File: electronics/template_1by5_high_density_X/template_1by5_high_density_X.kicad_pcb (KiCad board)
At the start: 2 copper layers, 19 x 41.5 mm, 14 parts, among them J1 1, J10 10, J11 11, J12 12, J2 2, J3 3, J4 4, J5 5, J6 6, J7 7, J8 8, J9 9

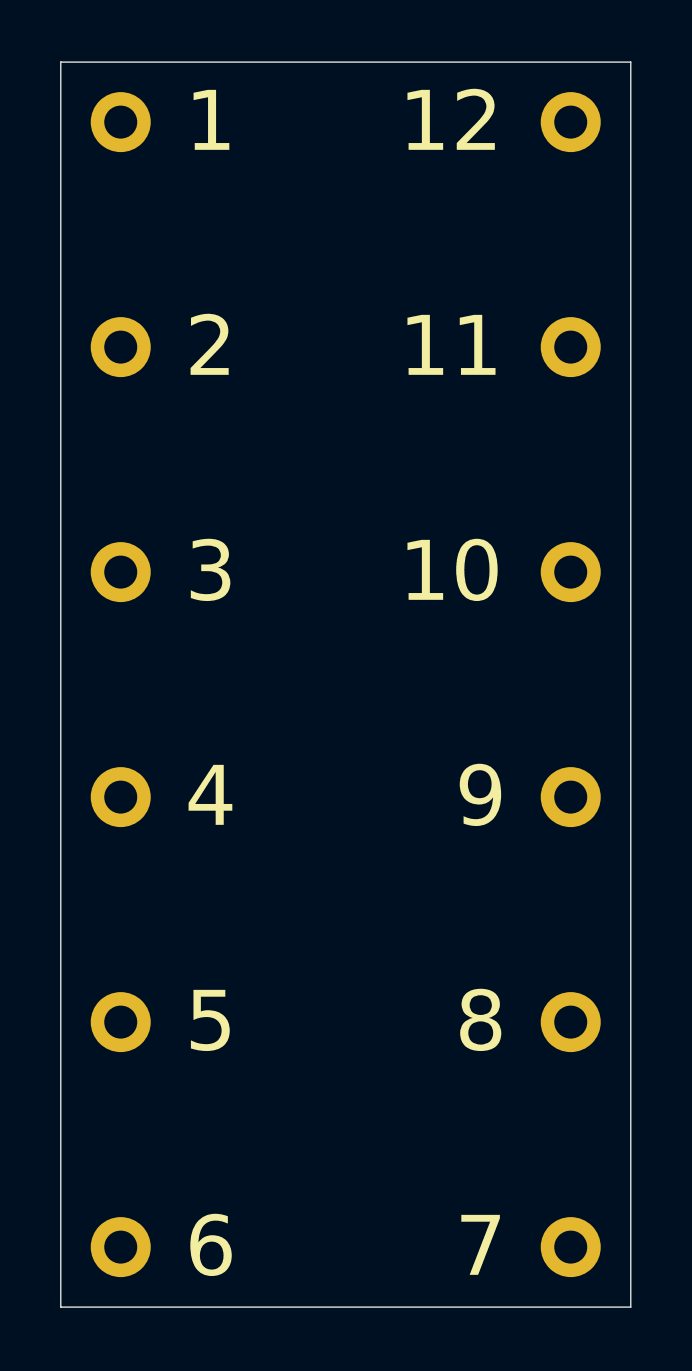
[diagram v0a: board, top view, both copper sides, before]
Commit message: completed high density X templates, updated versionnumbers of high density XN templates
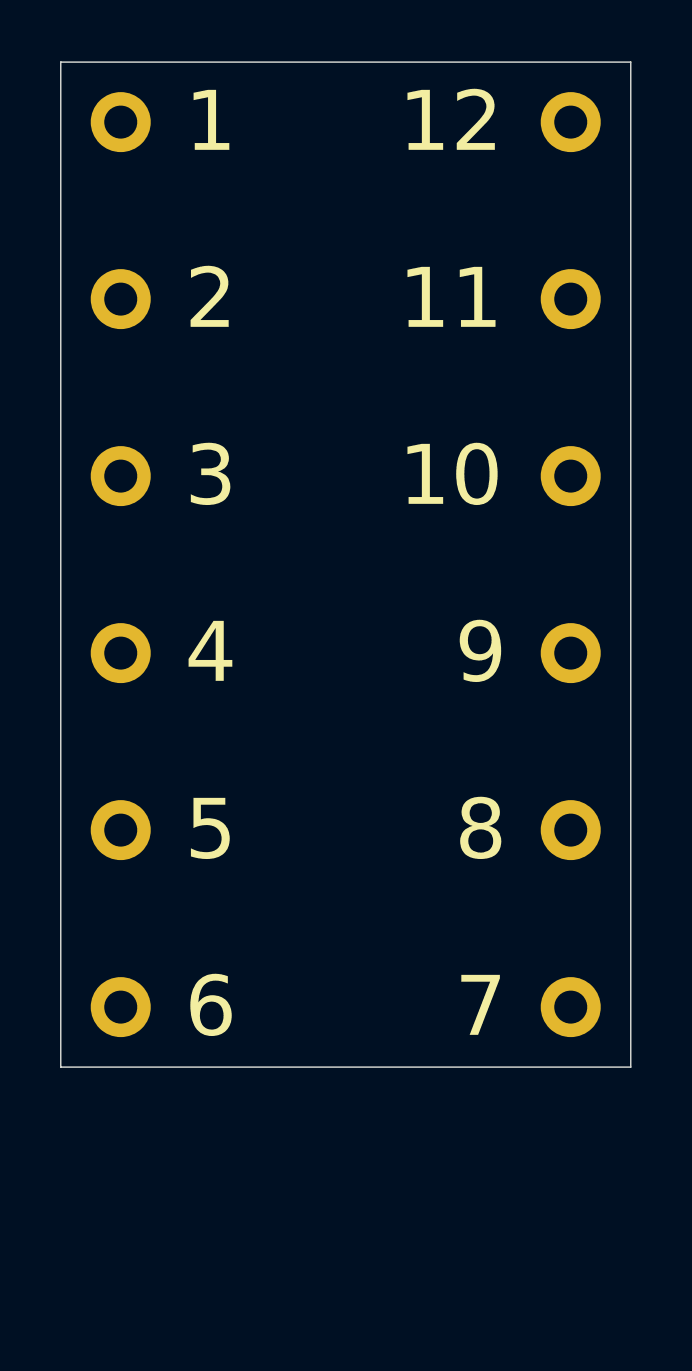
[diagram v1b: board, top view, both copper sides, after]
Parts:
- N1: value V20220113 -> V20240506
- moved J6 8.00 mm to (142.5, 92.0)
- moved J7 8.00 mm to (157.5, 92.0)
- moved J5 6.40 mm to (142.5, 86.1)
- moved J8 6.40 mm to (157.5, 86.1)
- moved J4 4.80 mm to (142.5, 80.2)
- moved J9 4.80 mm to (157.5, 80.2)
- moved J10 3.20 mm to (157.5, 74.3)
- moved J3 3.20 mm to (142.5, 74.3)
- moved J11 1.60 mm to (157.5, 68.4)
- moved J2 1.60 mm to (142.5, 68.4)
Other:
- board size 19 x 41.5 mm -> 19 x 33.5 mm
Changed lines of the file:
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@@
   (footprint "mill-max:PC_pin_nail_head_6092" locked (layer "F.Cu")
     (at 142.5 62.5)
-    (property "Sheetfile" "template_1by5.kicad_sch")
+    (property "Sheetfile" "template_1by5_high_density_X.kicad_sch")
     (property "Sheetname" "")
     (property "ki_description" "Generic connector, single row, 01x01, script generated (kicad-library-utils/schlib/autogen/connector/)")
@@
   )
   (footprint "mill-max:PC_pin_nail_head_6092" locked (layer "F.Cu")
-    (at 142.5 70)
-    (property "Sheetfile" "template_1by5.kicad_sch")
+    (at 142.5 68.4)
+    (property "Sheetfile" "template_1by5_high_density_X.kicad_sch")
     (property "Sheetname" "")
     (property "ki_description" "Generic connector, single row, 01x01, script generated (kicad-library-utils/schlib/autogen/connector/)")
@@
   )
   (footprint "mill-max:PC_pin_nail_head_6092" locked (layer "F.Cu")
-    (at 142.5 77.5)
-    (property "Sheetfile" "template_1by5.kicad_sch")
+    (at 142.5 74.3)
+    (property "Sheetfile" "template_1by5_high_density_X.kicad_sch")
     (property "Sheetname" "")
     (property "ki_description" "Generic connector, single row, 01x01, script generated (kicad-library-utils/schlib/autogen/connector/)")
@@
   )
   (footprint "mill-max:PC_pin_nail_head_6092" locked (layer "F.Cu")
-    (at 142.5 92.5 180)
-    (property "Sheetfile" "template_1by5.kicad_sch")
+    (at 142.5 86.1 180)
+    (property "Sheetfile" "template_1by5_high_density_X.kicad_sch")
     (property "Sheetname" "")
     (property "ki_description" "Generic connector, single row, 01x01, script generated (kicad-library-utils/schlib/autogen/connector/)")
@@
   )
   (footprint "mill-max:PC_pin_nail_head_6092" locked (layer "F.Cu")
-    (at 142.5 100 180)
-    (property "Sheetfile" "template_1by5.kicad_sch")
+    (at 142.5 92 180)
+    (property "Sheetfile" "template_1by5_high_density_X.kicad_sch")
     (property "Sheetname" "")
     (property "ki_description" "Generic connector, single row, 01x01, script generated (kicad-library-utils/schlib/autogen/connector/)")
@@
   )
   (footprint "mill-max:PC_pin_nail_head_6092" locked (layer "F.Cu")
-    (at 142.5 85 180)
-    (property "Sheetfile" "template_1by5.kicad_sch")
+    (at 142.5 80.2 180)
+    (property "Sheetfile" "template_1by5_high_density_X.kicad_sch")
     (property "Sheetname" "")
     (property "ki_description" "Generic connector, single row, 01x01, script generated (kicad-library-utils/schlib/autogen/connector/)")
@@
   )
   (footprint "mill-max:PC_pin_nail_head_6092" locked (layer "F.Cu")
-    (at 157.5 70)
-    (property "Sheetfile" "template_1by5.kicad_sch")
+    (at 157.5 68.4)
+    (property "Sheetfile" "template_1by5_high_density_X.kicad_sch")
     (property "Sheetname" "")
     (property "ki_description" "Generic connector, single row, 01x01, script generated (kicad-library-utils/schlib/autogen/connector/)")
@@
   )
   (footprint "mill-max:PC_pin_nail_head_6092" locked (layer "F.Cu")
-    (at 157.5 92.5)
-    (property "Sheetfile" "template_1by5.kicad_sch")
+    (at 157.5 86.1)
+    (property "Sheetfile" "template_1by5_high_density_X.kicad_sch")
     (property "Sheetname" "")
     (property "ki_description" "Generic connector, single row, 01x01, script generated (kicad-library-utils/schlib/autogen/connector/)")
@@
   )
   (footprint "mill-max:PC_pin_nail_head_6092" locked (layer "F.Cu")
-    (at 157.5 77.5)
-    (property "Sheetfile" "template_1by5.kicad_sch")
+    (at 157.5 74.3)
+    (property "Sheetfile" "template_1by5_high_density_X.kicad_sch")
     (property "Sheetname" "")
     (property "ki_description" "Generic connector, single row, 01x01, script generated (kicad-library-utils/schlib/autogen/connector/)")
@@
   )
   (footprint "mill-max:PC_pin_nail_head_6092" locked (layer "F.Cu")
-    (at 157.5 100)
-    (property "Sheetfile" "template_1by5.kicad_sch")
+    (at 157.5 92)
+    (property "Sheetfile" "template_1by5_high_density_X.kicad_sch")
     (property "Sheetname" "")
     (property "ki_description" "Generic connector, single row, 01x01, script generated (kicad-library-utils/schlib/autogen/connector/)")
@@
   )
   (footprint "mill-max:PC_pin_nail_head_6092" locked (layer "F.Cu")
-    (at 157.5 85)
-    (property "Sheetfile" "template_1by5.kicad_sch")
+    (at 157.5 80.2)
+    (property "Sheetfile" "template_1by5_high_density_X.kicad_sch")
     (property "Sheetname" "")
     (property "ki_description" "Generic connector, single row, 01x01, script generated (kicad-library-utils/schlib/autogen/connector/)")
@@
   (footprint "mill-max:PC_pin_nail_head_6092" locked (layer "F.Cu")
     (at 157.5 62.5)
-    (property "Sheetfile" "template_1by5.kicad_sch")
+    (property "Sheetfile" "template_1by5_high_density_X.kicad_sch")
     (property "Sheetname" "")
     (property "ki_description" "Generic connector, single row, 01x01, script generated (kicad-library-utils/schlib/autogen/connector/)")
@@
     (descr "Open Source Hardware Symbol")
     (tags "Logo Symbol OSHW")
-    (property "Sheetfile" "template_1by5.kicad_sch")
+    (property "Sheetfile" "template_1by5_high_density_X.kicad_sch")
     (property "Sheetname" "")
     (attr exclude_from_pos_files)
@@
     (descr "Label for general purpose use")
     (tags "Label")
-    (property "Sheetfile" "template_1by5.kicad_sch")
+    (property "Sheetfile" "template_1by5_high_density_X.kicad_sch")
     (property "Sheetname" "")
     (attr smd)
@@
         (effects (font (size 1 1) (thickness 0.15)) (justify mirror))
     )
-    (fp_text value "V20220113" (at 0.8 0.1) (layer "B.SilkS")
+    (fp_text value "V20240506" (at 0.8 0.1) (layer "B.SilkS")
         (effects (font (size 0.8 0.8) (thickness 0.15)) (justify mirror))
     )
@@
       (stroke (width 0.15) (type solid)) (layer "B.SilkS"))
   )
-  (gr_line (start 140.5 102) (end 159.5 102)
+  (gr_line (start 140.5 94) (end 159.5 94)
     (stroke (width 0.05) (type solid)) (layer "Edge.Cuts"))
-  (gr_line (start 159.5 60.5) (end 159.5 102)
+  (gr_line (start 159.5 60.5) (end 159.5 94)
     (stroke (width 0.05) (type solid)) (layer "Edge.Cuts"))
   (gr_line (start 159.5 60.5) (end 140.5 60.5)
     (stroke (width 0.05) (type solid)) (layer "Edge.Cuts"))
-  (gr_line (start 140.5 102) (end 140.5 60.5)
+  (gr_line (start 140.5 94) (end 140.5 60.5)
     (stroke (width 0.05) (type solid)) (layer "Edge.Cuts"))
 )
